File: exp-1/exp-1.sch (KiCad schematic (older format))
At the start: 125 parts, among them P2 CONN_2, P3 CONN_2, Q1 2n5109, Q2 MMBT3904T, Q3 MMBT3904T, Q4 DMP3099L, Q5 NPN, Q6 DMP3099L, U1 ABA-52563, U2 AVT-50663, U3 ABA-52563, U4 AVT-50663, U5 ADE-1, U6 Si570, U8 LM2937

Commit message: "Message goes here"
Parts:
- removed D3: DIODESCH, symbol DIODESCH
- removed Q2, Q3: MMBT3904T, symbol NPN
- removed Q4, Q6: DMP3099L, symbol MOSFET_P
- removed Q5: NPN, symbol NPN
- added C47, C48, C49: 22u, Capacitors_SMD:C_1206, symbol C
- added D3: BAT54C, Housings_SOT-23_SOT-143_TSOT-6:SOT-23, symbol DP2CA
- added P1: CONN_8, symbol CONN_8
- added Q2, Q3, Q5: MMBT3904T, Housings_SOT-23_SOT-143_TSOT-6:SOT-23, symbol MMBT3904T
- added Q4, Q6: DMP3099L, Housings_SOT-23_SOT-143_TSOT-6:SOT-23, symbol DMP3099L
- added U9: MCP1703T, symbol MCP1703T
- D4, D5, D6, D7: value BAV74 -> BAT54C
- R16, R17, R18, R19, R20, R21, R22, R23, R24, R25, R26, R27, R28, R29, R30, R31, R32: footprint (none) -> Resistors_SMD:R_0603_HandSoldering
- U7: renamed from U?; footprint (none) -> Housings_SSOP:TSSOP-16_4.4x5mm_Pitch0.65mm
- U8: footprint (none) -> SMD_Packages:SOT-223
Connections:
- wire segments 349 -> 367
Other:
- moved on the sheet: C20, C22, C45, R13, R14, R15, U6

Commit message: Continued work on that one thing
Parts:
- P1: footprint (none) -> exp-1:2x4_EDGE_.1
- U9: footprint (none) -> Housings_SOT-23_SOT-143_TSOT-6:SOT-23

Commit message: Schematic probably done. Layout still needs work
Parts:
- removed P2: CONN_2, symbol CONN_2
- added P2: BNC, Connect:bnc-ci, symbol BNC
- added P4: BNC, exp-1:TE_BNC_VERT, symbol BNC
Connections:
- wire segments 367 -> 371
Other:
- note added: "+11 db"
- note added: "+15 db"
- note added: "+21.5 dB"
- note added: "Control Connections"
- note added: "Filter verified in LTSpice"
- note added: "Fixed 2% chip inductors"
- note added: "Power Supply"
- note added: "TX Direct"
- note added: "TX Direct/ TX Switch selector\n"
- note added: "TX/RX"
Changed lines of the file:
@@
 encoding utf-8
 Sheet 1 1
-Title ""
+Title "VHF Front End"
 Date ""
-Rev ""
+Rev "1"
 Comp ""
 Comment1 ""
@@
 $EndComp
 $Comp
-L CONN_2 P2
-U 1 1 551DEF76
-P 4650 8300
-F 0 "P2" V 4600 8300 40  0000 C CNN
-F 1 "CONN_2" V 4700 8300 40  0000 C CNN
-F 2 "" H 4650 8300 60  0001 C CNN
-F 3 "" H 4650 8300 60  0000 C CNN
-	1    4650 8300
-	1    0    0    -1
-$EndComp
-$Comp
-L CONN_2 P3
-U 1 1 551DF928
-P 15200 9000
-F 0 "P3" V 15150 9000 40  0000 C CNN
-F 1 "CONN_2" V 15250 9000 40  0000 C CNN
-F 2 "" H 15200 9000 60  0001 C CNN
-F 3 "" H 15200 9000 60  0000 C CNN
-	1    15200 9000
-	1    0    0    -1
-$EndComp
-$Comp
 L INDUCTOR_C L13
 U 1 1 551E15CE
@@
 	4250 8500 4250 8400
 Wire Wire Line
-	4250 8400 4300 8400
+	4250 8400 4450 8400
 Wire Wire Line
 	2400 9400 2650 9400
@@
 	14700 8850 14700 8900
 Wire Wire Line
-	14700 8900 14850 8900
+	14700 8900 14950 8900
 Wire Wire Line
-	14600 9100 14850 9100
+	14600 9100 15100 9100
 Wire Wire Line
 	14700 8450 14700 8350
@@
 	11500 1300 11500 1700
 Wire Wire Line
-	10800 1000 11100 1000
+	10600 1000 11100 1000
 Wire Wire Line
 	11900 1000 12350 1000
@@
 	7600 4700 10100 4700
 Wire Notes Line
-	10100 4700 10100 6150
+	10100 4400 10100 6150
 Wire Notes Line
 	6650 8250 8400 8250
@@
 	15950 6150 15950 7450
 Wire Notes Line
-	10150 4400 10150 6100
+	14200 4400 14200 6150
 Wire Notes Line
-	10150 6100 14200 6100
-Wire Notes Line
-	14200 6100 14200 4400
-Wire Notes Line
-	14200 4400 10150 4400
+	10100 4400 14200 4400
 Wire Wire Line
 	1750 3300 2300 3300
@@
 	10950 1550 10950 1700
 Wire Wire Line
-	10950 1700 13450 1700
+	10600 1700 13450 1700
 Wire Wire Line
 	13450 1700 13450 1550
@@
 Wire Wire Line
 	12100 3250 12550 3250
+Text Notes 12150 2400 0    60   ~ 0
+Control Connections
+Wire Notes Line
+	11800 2200 11800 3500
+Wire Notes Line
+	11800 3500 13150 3500
+Wire Notes Line
+	13150 3500 13150 2200
+Wire Notes Line
+	13150 2200 11800 2200
+Text Notes 10950 750  0    60   ~ 0
+Power Supply
+Wire Notes Line
+	9850 2050 13750 2050
+Wire Notes Line
+	13750 2050 13750 550
+Wire Notes Line
+	13750 550  9850 550
+Text Notes 9900 7450 0    60   ~ 0
+Fixed 2% chip inductors
+Text Notes 11300 7450 0    60   ~ 0
+Filter verified in LTSpice
+Text Notes 9250 8850 0    60   ~ 0
++21.5 dB
+Text Notes 4950 5950 0    60   ~ 0
++21.5 dB
+Connection ~ 8150 7700
+Text Notes 6600 6350 0    60   ~ 0
++15 db
+Text Notes 10900 8850 0    60   ~ 0
++15 db
+Text Notes 13000 8850 0    60   ~ 0
++11 db
+$Comp
+L CONN_2 P3
+U 1 1 55233065
+P 10050 1450
+F 0 "P3" V 10000 1450 40  0000 C CNN
+F 1 "CONN_2" V 10100 1450 40  0000 C CNN
+F 2 "" H 10050 1450 60  0001 C CNN
+F 3 "" H 10050 1450 60  0000 C CNN
+	1    10050 1450
+	-1   0    0    1
+$EndComp
+Wire Notes Line
+	9850 550  9850 2050
+Wire Wire Line
+	10600 1000 10600 1350
+Wire Wire Line
+	10600 1350 10400 1350
+Wire Wire Line
+	10400 1550 10600 1550
+Wire Wire Line
+	10600 1550 10600 1700
+Connection ~ 10950 1700
+$Comp
+L BNC P4
+U 1 1 55235DD1
+P 15100 8900
+F 0 "P4" H 15110 9020 60  0000 C CNN
+F 1 "BNC" V 15210 8840 40  0000 C CNN
+F 2 "exp-1:TE_BNC_VERT" H 15100 8900 60  0001 C CNN
+F 3 "" H 15100 8900 60  0000 C CNN
+	1    15100 8900
+	1    0    0    -1
+$EndComp
+$Comp
+L BNC P2
+U 1 1 55236B7F
+P 4450 8200
+F 0 "P2" H 4460 8320 60  0000 C CNN
+F 1 "BNC" V 4560 8140 40  0000 C CNN
+F 2 "Connect:bnc-ci" H 4450 8200 60  0001 C CNN
+F 3 "" H 4450 8200 60  0000 C CNN
+	1    4450 8200
+	1    0    0    -1
+$EndComp
+Text Notes 14100 8200 0    60   ~ 0
+TX Direct/ TX Switch selector\n
+Text Notes 14900 8700 0    60   ~ 0
+TX Direct
+Text Notes 4300 8000 0    60   ~ 0
+TX/RX
 $EndSCHEMATC

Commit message: Further work on that one thing
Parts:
- P2: footprint Connect:bnc-ci -> exp-1:SMA_EMNT
- P4: footprint exp-1:TE_BNC_VERT -> exp-1:SMA_EMNT
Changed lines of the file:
@@
 F 0 "P4" H 15110 9020 60  0000 C CNN
 F 1 "BNC" V 15210 8840 40  0000 C CNN
-F 2 "exp-1:TE_BNC_VERT" H 15100 8900 60  0001 C CNN
+F 2 "exp-1:SMA_EMNT" H 15100 8900 60  0001 C CNN
 F 3 "" H 15100 8900 60  0000 C CNN
 	1    15100 8900
@@
 F 0 "P2" H 4460 8320 60  0000 C CNN
 F 1 "BNC" V 4560 8140 40  0000 C CNN
-F 2 "Connect:bnc-ci" H 4450 8200 60  0001 C CNN
+F 2 "exp-1:SMA_EMNT" H 4450 8200 60  0001 C CNN
 F 3 "" H 4450 8200 60  0000 C CNN
 	1    4450 8200

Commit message: Added the rest of the connectors
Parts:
- added P5: CONN_2, Pin_Headers:Pin_Header_Straight_1x02, symbol CONN_2
- P2, P4: value BNC -> SMA; P (none) -> 73251-1150
- P3: footprint (none) -> Pin_Headers:Pin_Header_Straight_1x02
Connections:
- wire segments 371 -> 373
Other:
- note added: "IF connection"

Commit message: Further work on schematic rework.
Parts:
- removed C11: 15p, Capacitors_SMD:C_0603_HandSoldering, symbol C
- removed C13, C23: 470p, Capacitors_SMD:C_0603_HandSoldering, symbol C
- removed C14, C21, C24, C25, C27, C32: .01u, Capacitors_SMD:C_0603_HandSoldering, symbol C
- removed D1, D2: BAR15-1, Housings_SOT-23_SOT-143_TSOT-6:SOT-23, symbol DP2CA
- removed D4, D5, D6, D7: BAT54C, Housings_SOT-23_SOT-143_TSOT-6:SOT-23, symbol DP2CA
- removed FB2: FILTER, Choke_SMD:Choke_SMD_1206_Handsoldering, symbol FILTER
- removed L11: 100n, Resistors_SMD:R_0603, symbol INDUCTOR_C
- removed L13, L14, L15, L5, L6, L7: .33u, Resistors_SMD:R_0603, symbol INDUCTOR_C
- removed Q1: 2n5109, Discret:TO39EBC, symbol NPN
- removed Q3: MMBT3904T, Housings_SOT-23_SOT-143_TSOT-6:SOT-23, symbol MMBT3904T
- removed R1, R8: 680R, Resistors_SMD:R_0603_HandSoldering, symbol RA
- removed R17, R5: 1K, Resistors_SMD:R_0603_HandSoldering, symbol RA
- removed R19: 10K, Resistors_SMD:R_0603_HandSoldering, symbol RA
- removed R2, R9: 121R, Resistors_SMD:R_0603_HandSoldering, symbol RA
- removed R21: 1k, Resistors_SMD:R_0603_HandSoldering, symbol RA
- removed R25, R29: 300, Resistors_SMD:R_0603_HandSoldering, symbol RA
- removed R26, R30: 6.2k, Resistors_SMD:R_0603_HandSoldering, symbol RA
- removed R27, R31: 20k, Resistors_SMD:R_0603_HandSoldering, symbol RA
- removed R28, R32: 47k, Resistors_SMD:R_0603_HandSoldering, symbol RA
- removed R4: 3.3k, Resistors_SMD:R_0603_HandSoldering, symbol RA
- removed R6: 2.2R, Resistors_SMD:R_0603_HandSoldering, symbol RA
- removed R7: 22R, Resistors_SMD:R_0603_HandSoldering, symbol RA
- removed U7: 74HC595_, Housings_SSOP:TSSOP-16_4.4x5mm_Pitch0.65mm, symbol 74HC595_
- added C?: 470p, Capacitors_SMD:C_0603_HandSoldering, symbol C
- added C? (x2): .01u, Capacitors_SMD:C_0603_HandSoldering, symbol C
- added U? (x2): AS179-92LF, symbol SKY13351
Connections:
- net labels removed: RATT2, RATT_1, RATT_2, VATEN
- wire segments 373 -> 278
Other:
- note removed: "+11 db"
- note removed: "RX Attenuation control.\nResistors adjusted for 3.3v\ndiode drop may be a problem"
- moved on the sheet: C26, C28, C29, C30, C36, C38, FILT3, L12, P2, P4, SL1

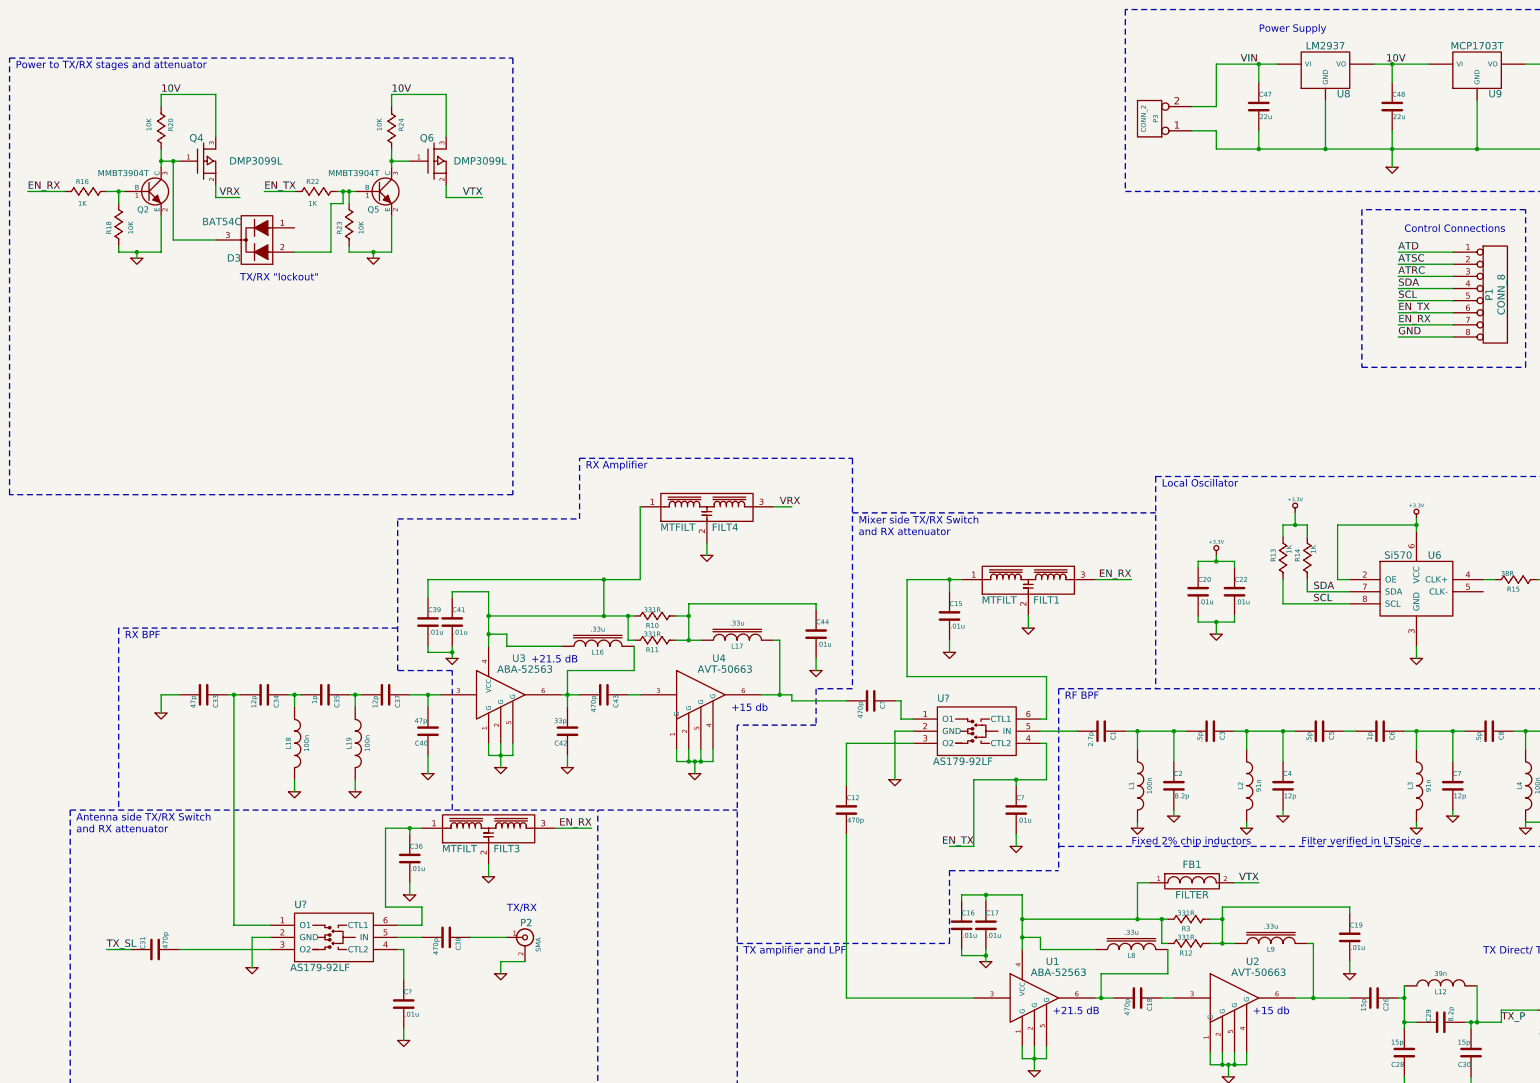
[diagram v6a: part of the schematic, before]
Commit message: Replaced power switching with canned switch. Changed 10v regulator to 5v.
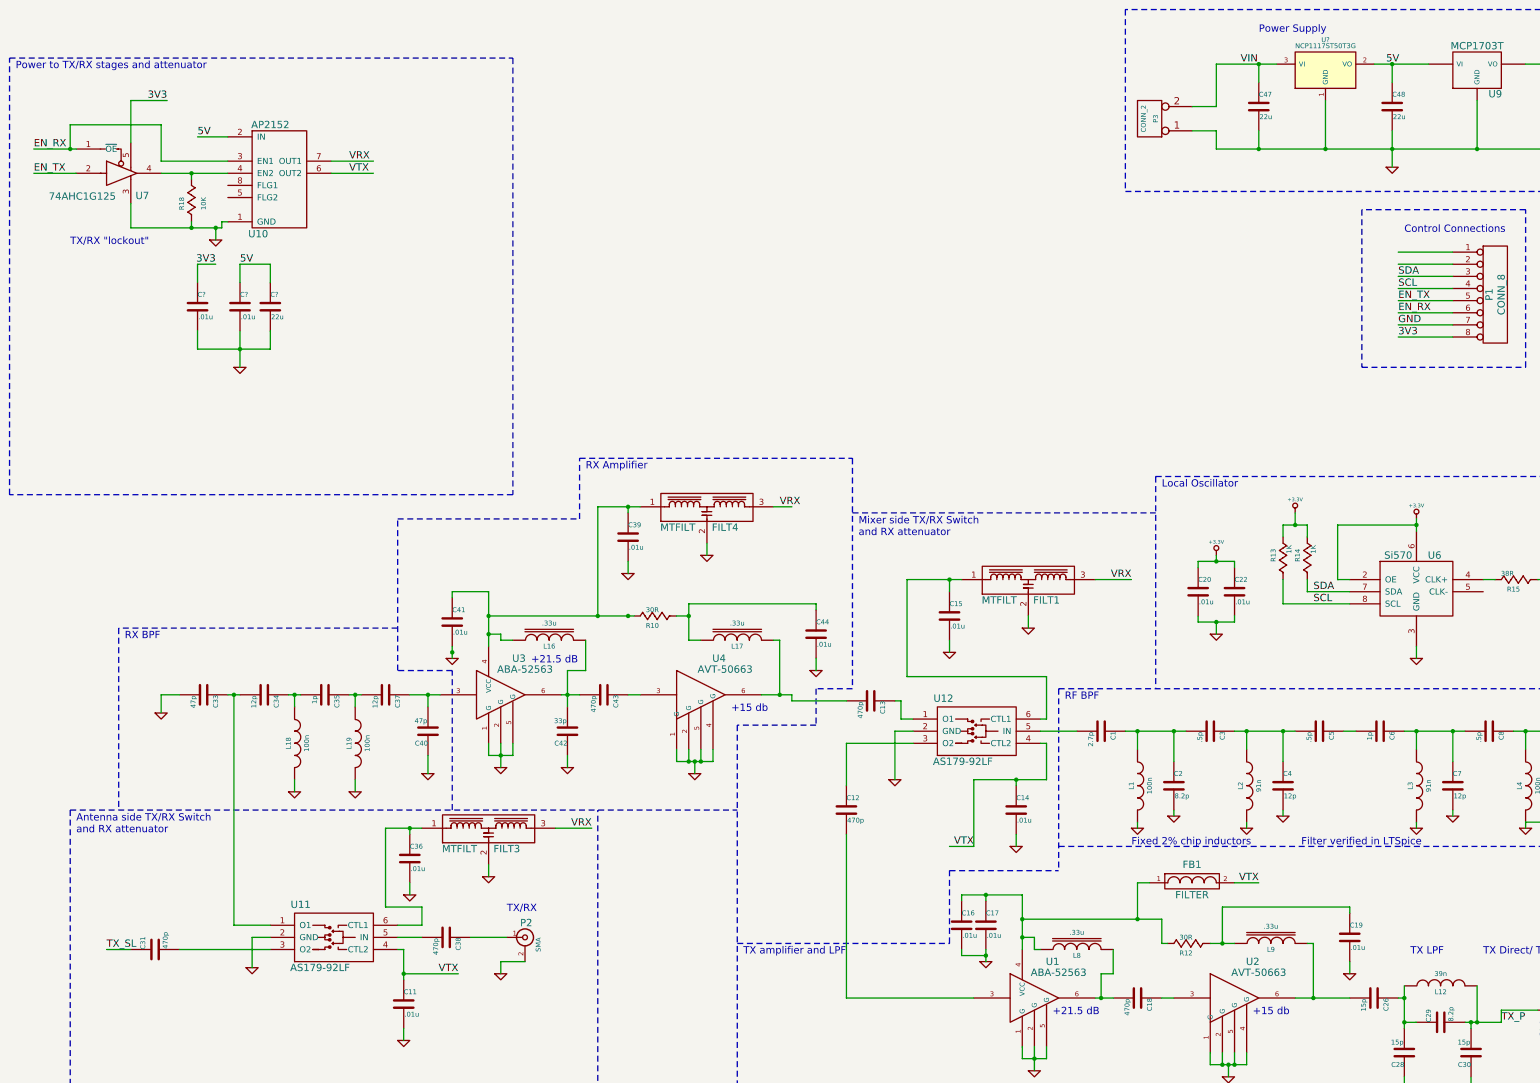
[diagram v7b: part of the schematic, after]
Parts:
- removed D3: BAT54C, Housings_SOT-23_SOT-143_TSOT-6:SOT-23, symbol DP2CA
- removed Q2, Q5: MMBT3904T, Housings_SOT-23_SOT-143_TSOT-6:SOT-23, symbol MMBT3904T
- removed Q4, Q6: DMP3099L, Housings_SOT-23_SOT-143_TSOT-6:SOT-23, symbol DMP3099L
- removed R11, R3: 331R, Resistors_SMD:R_0603_HandSoldering, symbol RA
- removed R16, R22: 1K, Resistors_SMD:R_0603_HandSoldering, symbol RA
- removed R20, R23, R24: 10K, Resistors_SMD:R_0603_HandSoldering, symbol RA
- removed U8: LM2937, SMD_Packages:SOT-223, symbol LM2937
- added C? (x2): .01u, Capacitors_SMD:C_0603_HandSoldering, symbol C
- added C?: 22u, Capacitors_SMD:C_1206, symbol C
- added U10: AP2152, SMD_Packages:SOIC-8-N, symbol AP2152
- added U7: 74AHC1G125, SMD_Packages:SOT-353, symbol 74AHC1G125
- added U?: NCP1117ST50T3G, symbol NCP1117ST50T3G
- R10, R12: value 331R -> 30R
- U11, U12: renamed from U?; footprint (none) -> exp-1:SOT_363
- gave numbers to parts that had none: 3
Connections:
- net ATRC is gone; now on net SDA: P1.3 (P3)
- net EN_RX: now also P1.6 (P6), U10.3 (EN1), U7.1 (~OE); no longer FILT1.3, FILT3.3, P1.7 (P7)
- net EN_TX: now also P1.5 (P5), U7.2; no longer C14.1, P1.6 (P6), U12.4 (CTL2)
- net GND: now also P1.7 (P7), C?.2, C?.2, C?.2, U10.1 (GND), U7.3, U?.1 (GND); no longer P1.8 (P8)
- net SCL: now also P1.4 (P4); no longer P1.5 (P5)
- net SDA: no longer P1.4 (P4)
- net VIN: now also U?.3 (VI)
- net VRX: now also FILT1.3, FILT3.3, U10.7 (OUT1)
- net VTX: now also C11.1, C14.1, U11.4 (CTL2), U12.4 (CTL2), U10.6 (OUT2)
- net at R18.2: now also U10.4 (EN2), U7.4
- net 10V renamed 5V
- net 5V: now also C?.1, C?.1, U10.2 (IN), U?.2 (VO)
- net ATD: no longer names the net of P1.1 (P1)
- net ATSC: no longer names the net of P1.2 (P2)
- new net 3V3: C?.1, P1.8 (P8), U7.5
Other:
- note added: "TX LPF"
- moved on the sheet: C39, L16, L8, R18

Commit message: Updated PDF
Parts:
- added P6, P7, P8: U.FL, exp-1:A-1JB, symbol BNC
- added R1, R2: 10K, Resistors_SMD:R_0603_HandSoldering, symbol RA
- added R3, R4, R5: 0R, Resistors_SMD:R_0805_HandSoldering, symbol RA
- C1, C10, C11, C12, C13, C14, C15, C16, C17, C18, C19, C2, C20, C22, C26, C28, C29, C3, C30, C31, C33, C34, C35, C36, C37, C38, C39, C4, C40, C41, C42, C43, C44, C45, C46, C47, C48, C49, C5, C6, C7, C8, C9: symbol C -> C-RESCUE-exp-1
- C21, C23, C24: renamed from C?; symbol C -> C-RESCUE-exp-1
- U6: symbol Si570 -> Si570-RESCUE-exp-1
- U8: renamed from U?; footprint (none) -> SMD_Packages:SOT-223
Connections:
- net EN_RX: now also R1.2
- net EN_TX: now also R2.2
- net GND: now also P6.2 (Ext), P7.2 (Ext), P8.2 (Ext), R1.1, R2.1
- net VTX: now also U11.6 (CTL1); no longer U11.4 (CTL2)
- net at C1.2, U12.5 (IN): now also R3.2
- net at C10.1, U5.3 (RF): now also R5.2
- net at C33.1, C34.2: now also U11.3 (O2); no longer U11.1 (O1)
- net at C36.1, FILT3.1: now also U11.4 (CTL2); no longer U11.6 (CTL1)
- net at C31.2: now also U11.1 (O1); no longer U11.3 (O2)
- net at C45.2, R15.1: now also R4.1
- new net: P7.1 (In), R4.2
- new net: P8.1 (In), R5.1
- new net: P6.1 (In), R3.1
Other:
- note added: "Ext. Filt"
- note added: "Ext. LO"
- moved on the sheet: C21, C23, C24, R18, U10, U7
